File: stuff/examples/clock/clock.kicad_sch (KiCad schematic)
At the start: 34 parts, among them SW1 SWITCH, SW2 SWITCH, U1 74LS393, U1 MAX7375AXR805, U10 4543, U11 4543, U12 4543, U13 4069, U14 4081, U15 HDSP-A153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

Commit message: clock example - blinking second point.
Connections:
- net at U1.4 (Q1), U4.1 (CK): now also U17.7 (DP)
- no-connect marks 68 -> 67
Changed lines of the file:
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@@
   (junction (at 191.77 107.95) (diameter 0) (color 0 0 0 0)
+  )
+  (junction (at 60.325 96.52) (diameter 0) (color 0 0 0 0)
   )
   (junction (at 114.3 135.89) (diameter 0) (color 0 0 0 0)
@@
   (no_connect (at 116.205 146.05))
   (no_connect (at 238.125 56.515))
-  (no_connect (at 141.605 115.57))
   (no_connect (at 55.245 121.92))
   (no_connect (at 225.425 74.295))
@@
   (no_connect (at 116.205 44.45))
   (no_connect (at 116.205 41.91))
+  (wire (pts (xy 141.605 115.57) (xy 141.605 121.92))
+    (stroke (width 0) (type default))
+  )
   (wire (pts (xy 225.425 110.49) (xy 220.98 110.49))
     (stroke (width 0) (type default))
@@
     (stroke (width 0) (type default))
   )
+  (wire (pts (xy 62.865 96.52) (xy 60.325 96.52))
+    (stroke (width 0) (type default))
+  )
   (wire (pts (xy 76.835 83.82) (xy 67.31 83.82))
     (stroke (width 0) (type default))
@@
     (stroke (width 0) (type default))
   )
+  (wire (pts (xy 141.605 121.92) (xy 62.865 121.92))
+    (stroke (width 0) (type default))
+  )
   (wire (pts (xy 24.765 175.26) (xy 24.765 162.56))
     (stroke (width 0) (type default))
@@
     (stroke (width 0) (type default))
   )
+  (wire (pts (xy 60.325 34.29) (xy 60.325 96.52))
+    (stroke (width 0) (type default))
+  )
   (wire (pts (xy 74.93 161.29) (xy 76.2 161.29))
     (stroke (width 0) (type default))
@@
     (stroke (width 0) (type default))
   )
-  (wire (pts (xy 60.325 34.29) (xy 60.325 96.52))
-    (stroke (width 0) (type default))
-  )
   (wire (pts (xy 191.77 120.015) (xy 191.77 107.95))
     (stroke (width 0) (type default))
   )
+  (wire (pts (xy 62.865 121.92) (xy 62.865 96.52))
+    (stroke (width 0) (type default))
+  )

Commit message: cleanup
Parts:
- added unit 3 of U4
- U1: SymPartParam freq=16.384;start -> (none)
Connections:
- new net gnd: U4.8 (VSS)
- new net pwr: U4.16 (VDD)

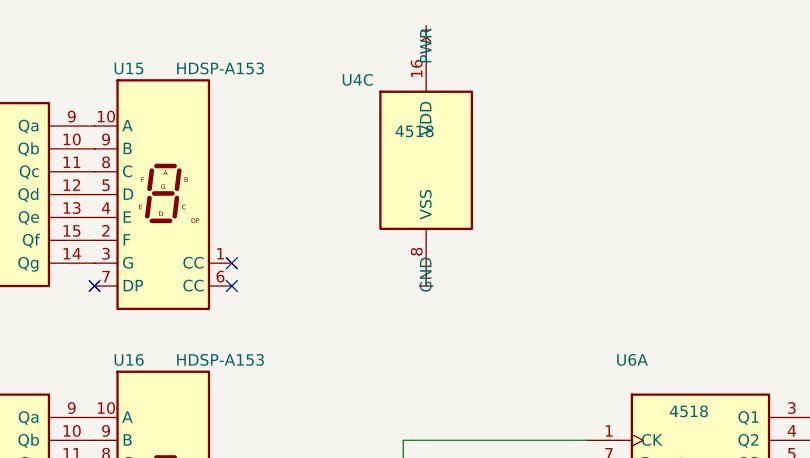
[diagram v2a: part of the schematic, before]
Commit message: preserve ignored units in Schema part instance from mapping file
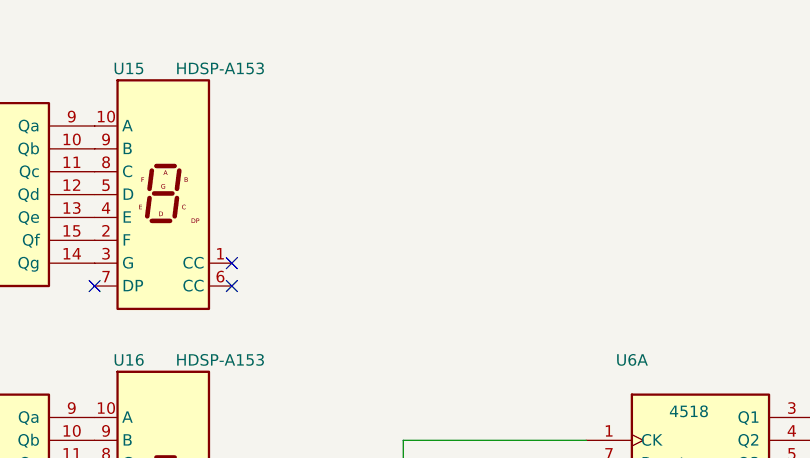
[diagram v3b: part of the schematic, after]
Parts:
- removed unit 3 of U4
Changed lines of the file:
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@@
-    )
-  )
-  (symbol (lib_id "4xxx:4518") (at 178.435 35.56 0) (unit 3)
-    (in_bom yes) (on_board yes) (dnp no)
-    (property "Reference" "U4" (at 170.815 26.67 0)
-      (effects (font (size 1.27 1.27)))
-    )
-    (property "Value" "4518" (at 177.165 32.385 0)
-      (effects (font (size 1.27 1.27)))
-    )
-    (property "Footprint" "" (at 178.435 35.56 0)
-      (effects (font (size 1.27 1.27)) hide)
-    )
-    (property "Datasheet" "http://www.intersil.com/content/dam/Intersil/documents/cd45/cd4518bms-20bms.pdf" (at 178.435 35.56 0)
-      (effects (font (size 1.27 1.27)) hide)
-    )
-    (pin "5")
-    (pin "10")
-    (pin "1")
-    (pin "14")
-    (pin "15")
-    (pin "6")
-    (pin "8")
-    (pin "16")
-    (pin "2")
-    (pin "9")
-    (pin "4")
-    (pin "3")
-    (pin "7")
-    (pin "13")
-    (pin "11")
-    (pin "12")
-    (instances
-      (project "clock"
-        (path "/b79032c5-346d-4cc4-b6ed-12df81e05ffd"
-          (reference "U4") (unit 3)
-        )
-      )
     )
   )
@@
         )
       )
-    )
-  )
-  (symbol (lib_id "chip:GND") (at 178.435 48.26 90) (unit 1)
-    (in_bom no) (on_board no) (dnp no)
-    (property "Reference" "#GND01" (at 179.705 54.61 0)
-      (effects (font (size 1.27 1.27)) hide)
-    )
-    (property "Value" "GND" (at 178.435 48.26 0)
-      (effects (font (size 0 0)))
-    )
-    (property "Footprint" "" (at 180.975 51.816 0)
-      (effects (font (size 1.27 1.27)) hide)
-    )
-    (property "Datasheet" "" (at 180.975 51.816 0)
-      (effects (font (size 1.27 1.27)) hide)
-    )
-    (pin "1")
-    (instances
-      (project "clock"
-        (path "/b79032c5-346d-4cc4-b6ed-12df81e05ffd"
-          (reference "#GND01") (unit 1)
-        )
-      )
-    )
-  )
-  (symbol (lib_id "chip:PWR") (at 178.435 22.86 270) (unit 1)
-    (in_bom no) (on_board no) (dnp no)
-    (property "Reference" "#PWR01" (at 177.165 16.51 0)
-      (effects (font (size 1.27 1.27)) hide)
-    )
-    (property "Value" "PWR" (at 178.435 22.86 0)
-      (effects (font (size 0 0)))
-    )
-    (property "Footprint" "" (at 175.895 19.304 0)
-      (effects (font (size 1.27 1.27)) hide)
-    )
-    (property "Datasheet" "" (at 175.895 19.304 0)
-      (effects (font (size 1.27 1.27)) hide)
-    )
-    (pin "1")
-    (instances
-      (project "clock"
-        (path "/b79032c5-346d-4cc4-b6ed-12df81e05ffd"
-          (reference "#PWR01") (unit 1)
-        )
-      )
